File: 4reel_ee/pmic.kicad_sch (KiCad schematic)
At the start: 35 parts, among them U2 EA3036C, U4 TLV73312PDBV, U6 TLV73328PDBV

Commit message: Rename
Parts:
- U2: symbol wingcam:EA3036C -> 4reel:EA3036C

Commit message: R0.1-rc1
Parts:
- C1, C14, C15, C16: MPN (none) -> CL05B104KP5VPNC
- C10, C12, C13, C2, C3, C4, C5, C7, C9: MPN (none) -> GRM155R60J106ME05D
- C11, C6, C8: MPN (none) -> GCM1555C1H221JA16D
- C29, C30, C33, C34: MPN (none) -> C0402C105K9PACTU
- L1, L2, L3: footprint (none) -> Inductor_SMD:L_1008_2520Metric; MPN (none) -> DFE252012P-1R5M=P2
- R1: MPN (none) -> RC0402FR-0740K2L
- R2: MPN (none) -> RC0402FR-079K1L
- R3: MPN (none) -> RC0402FR-0747KL
- R4, R6, R9: MPN (none) -> RC0402FR-07100KL
- R5, R7: MPN (none) -> RC0402FR-07200KL
- R8: MPN (none) -> RC0402FR-0710KL
- U2: MPN (none) -> EA3036C
- U4: MPN (none) -> TLV73312PDBV
- U6: MPN (none) -> TLV73328PDBVR

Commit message: R0.1 release.
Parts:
- U2: MPN EA3036C -> EA3036CQBR
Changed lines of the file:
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@@
 			)
 		)
-		(property "MPN" "EA3036C"
+		(property "MPN" "EA3036CQBR"
 			(at 69.85 69.85 0)
 			(hide yes)

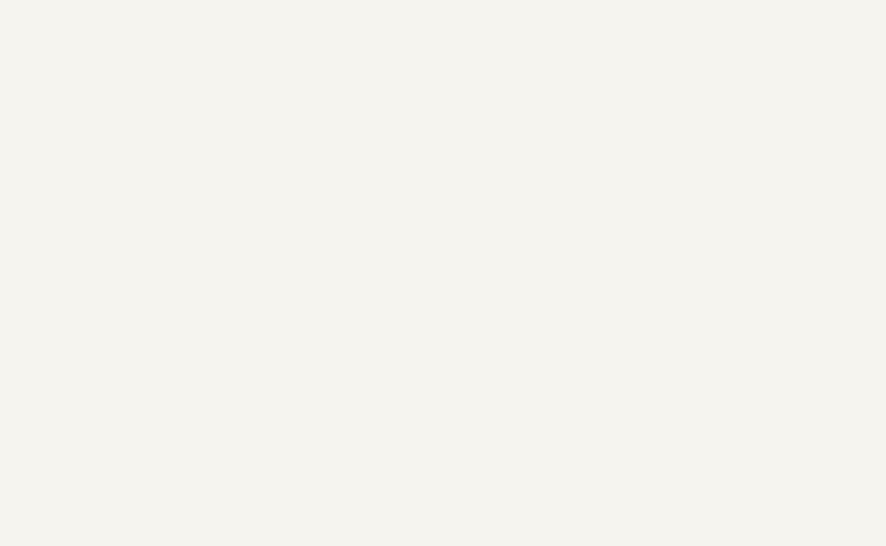
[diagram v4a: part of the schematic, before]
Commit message: Initial schematic, routing finished for RV1106 based design.
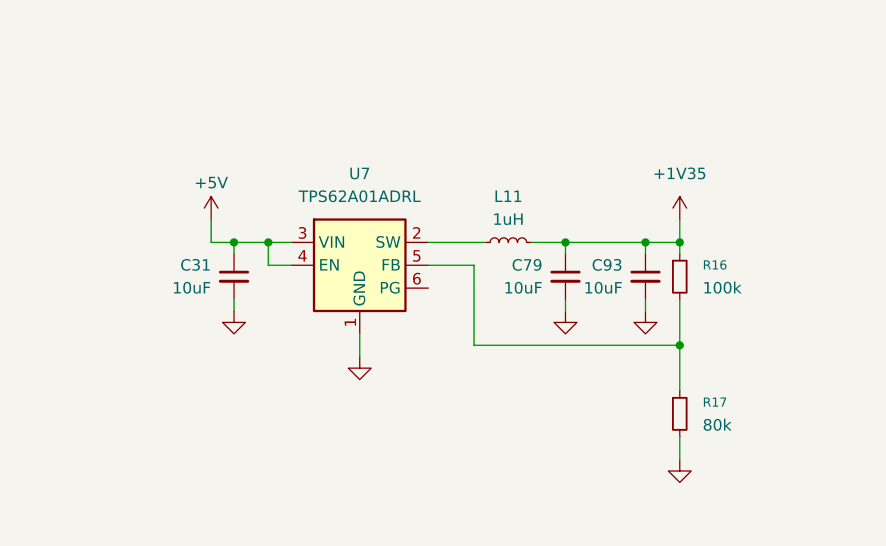
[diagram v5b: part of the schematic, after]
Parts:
- added C31, C79, C93: 10uF, Capacitor_SMD:C_0402_1005Metric, symbol Device:C_Small
- added L11: 1uH, Inductor_SMD:L_1008_2520Metric, symbol Device:L_Small
- added R16: 100k, Resistor_SMD:R_0402_1005Metric, symbol Device:R_Small
- added R17: 80k, Resistor_SMD:R_0402_1005Metric, symbol Device:R_Small
- added U7: TPS62A01ADRL, Package_TO_SOT_SMD:SOT-563, symbol Regulator_Switching:TPS62A01ADRL
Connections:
- net +5V: now also C31.1, U7.3 (VIN), U7.4 (EN)
- net GND: now also C31.2, C79.2, C93.2, R17.2, U7.1 (GND)
- new net: L11.1, U7.2 (SW)
- new net: R16.2, R17.1, U7.5 (FB)
- new net +1V35: C79.1, C93.1, L11.2, R16.1
